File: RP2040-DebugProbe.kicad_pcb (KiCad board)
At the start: 2 copper layers, 60 parts, among them J1 CONN_MCU_JTAG, J10 CONN_USB, J2 CONN_MCU_UART, J3 CONN_DBG_COMB, J4 CONN_3V3_JUMPER, J7 CONN_DBG_JTAG, SW1 BOOTSEL, U1 W25Q128JVS, U2 RP2040, U3 74AUP1T17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

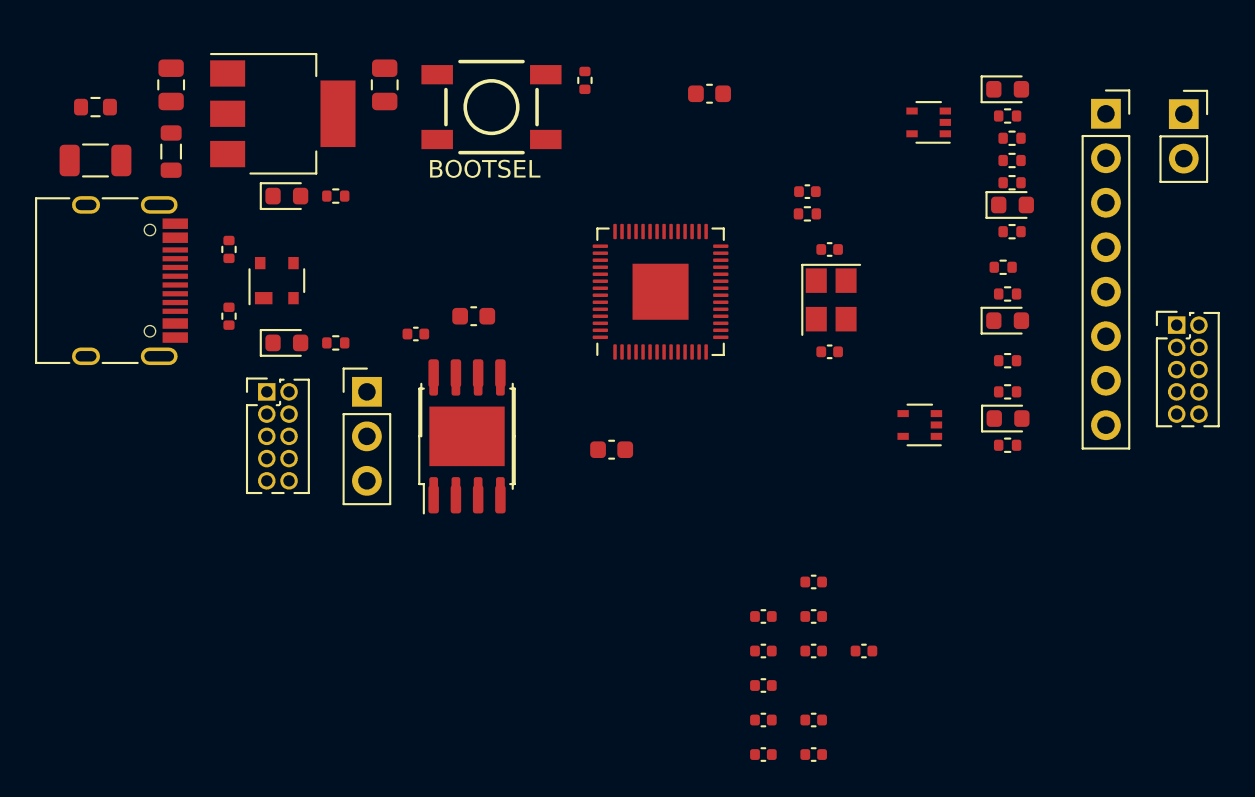
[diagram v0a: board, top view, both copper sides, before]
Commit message: Placed components on their approximate locations. Added board approximate outline.
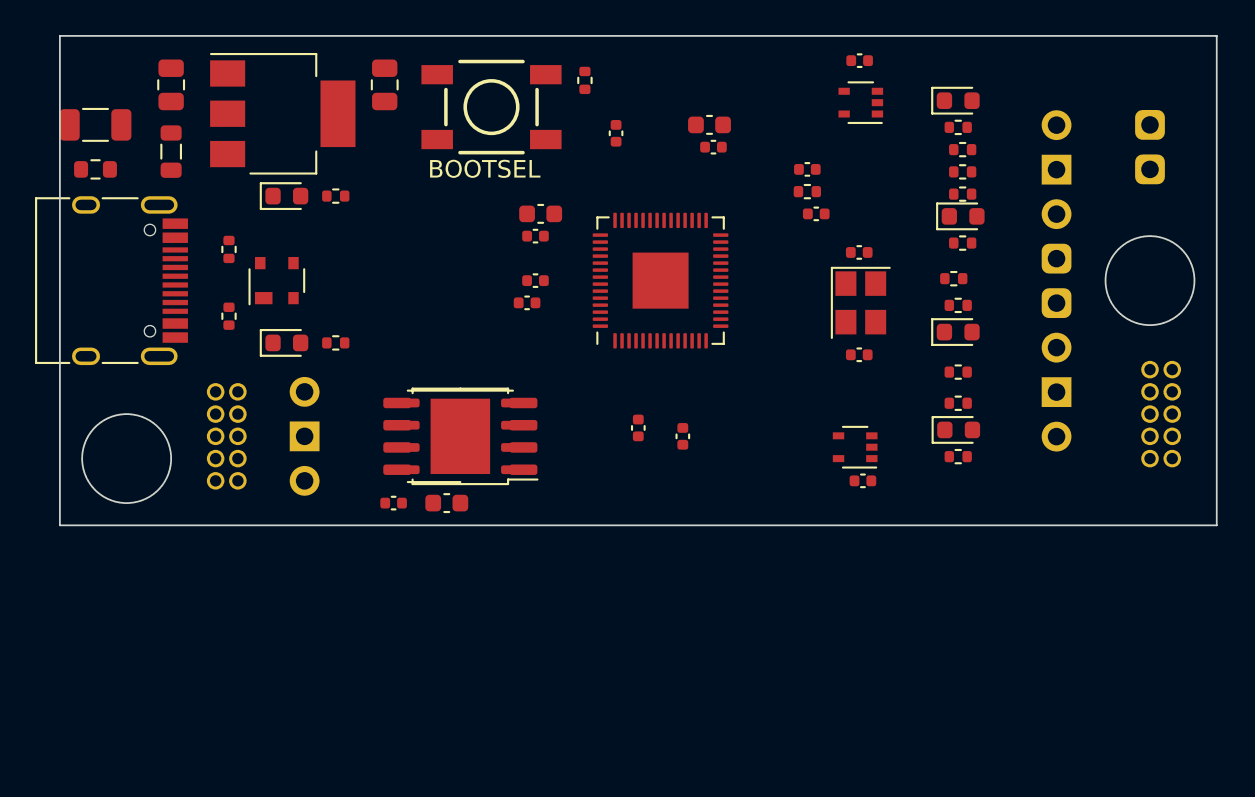
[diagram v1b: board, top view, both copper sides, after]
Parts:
- removed C22: 100nF, Capacitor_SMD:C_0402_1005Metric
- J3: footprint Connector_PinSocket_2.54mm:PinSocket_1x08_P2.54mm_Vertical -> Connector_PinHeader_2.54mm:PinHeader_1x08_P2.54mm_Vertical
- J4: footprint Connector_PinSocket_2.54mm:PinSocket_1x02_P2.54mm_Vertical -> Connector_PinHeader_2.54mm:PinHeader_1x02_P2.54mm_Vertical
- moved C17 39.7 mm to (170.1, 95.4)
- moved C6 32.6 mm to (156.2, 99.5), turned to 90 degrees
- moved C7 30.5 mm to (151.6, 105.4), turned to 180 degrees
- moved C8 30.0 mm to (151.6, 108.0), turned to 180 degrees
- moved C4 28.9 mm to (161.8, 100.3)
- moved C11 25.0 mm to (167.6, 104.1)
- moved C9 22.8 mm to (151.1, 109.2), turned to 180 degrees
- moved C5 14.1 mm to (151.9, 104.1), turned to 180 degrees
- moved C13 13.9 mm to (170.3, 119.4)
- moved C3 12.9 mm to (157.5, 116.4), turned to -90 degrees
- moved C10 12.7 mm to (160.0, 116.8), turned to -90 degrees
- moved C16 10.8 mm to (146.5, 120.7)
- moved C2 9.74 mm to (143.5, 120.7)
- moved J7 7.62 mm to (188.0, 118.1), turned to 180 degrees
- moved J1 5.34 mm to (134.6, 119.4), turned to 180 degrees
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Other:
- board outline added: 66 x 27.9 mm

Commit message: Moved stuff around
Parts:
- added C18: 100nF, Capacitor_SMD:C_0402_1005Metric, F.Cu at (164.5, 104.1)
- moved C1 17.5 mm to (158.1, 116.2), turned to -90 degrees
- moved R13 9.75 mm to (169.5, 115.6)
- moved C6 7.34 mm to (150.5, 104.1), turned to 180 degrees
- moved J7 6.99 mm to (181.0, 118.1)
- moved J3 6.73 mm to (174.6, 99.1)
- moved R15 6.60 mm to (169.5, 100.3)
- moved R9 6.55 mm to (169.5, 101.6)
- moved D1 6.48 mm to (169.5, 104.1)
- moved R1 6.46 mm to (169.5, 105.4), turned to 0 degrees
- moved R14 6.45 mm to (169.5, 102.9)
- moved R2 6.36 mm to (169.5, 97.8)
- moved J4 6.35 mm to (180.3, 99.1)
- moved D4 6.35 mm to (169.5, 99.1)
- moved R5 6.32 mm to (169.4, 118.1)
- moved R4 6.30 mm to (169.5, 110.5)
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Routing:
- net VUSB: track 0.00 -> 56.0 mm, vias 0 -> 1
- net +3V3: track 0.00 -> 48.5 mm, vias 0 -> 6
- net +1V1: track 0.00 -> 37.3 mm, vias 0 -> 3
- net QSPI_SS: track 0.00 -> 25.4 mm, vias 0 -> 2
- net USB_DP: track 0.00 -> 24.7 mm, vias 0 -> 2
- net USB_DN: track 0.00 -> 24.6 mm
- net VBUS: track 0.00 -> 20.6 mm, vias 0 -> 4
- net TARGET_3V3: track 0.00 -> 19.5 mm
- net QSPI_SD3: track 0.00 -> 16.6 mm
- net QSPI_SCLK: track 0.00 -> 14.5 mm
- net TARGET_CLK: track 0.00 -> 12.3 mm
- net SHIELD: track 0.00 -> 12.2 mm, vias 0 -> 1
- net TARGET_DIO: track 0.00 -> 12.0 mm
- net QSPI_SD0: track 0.00 -> 9.89 mm
- net XIN: track 0.00 -> 9.85 mm
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- added copper zone on B.Cu, net GND
- added copper zone on F.Cu, net GND
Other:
- board size 66 x 27.9 mm -> 59.7 x 25.4 mm

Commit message: Moved stuff around
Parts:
- moved C21 20.1 mm to (133.3, 117.5), turned to -90 degrees
- moved C1 14.6 mm to (157.5, 101.6), turned to 0 degrees
- moved R12 14.2 mm to (133.3, 114.3), turned to 0 degrees
- moved R3 11.4 mm to (130.2, 114.9)
- moved R6 11.4 mm to (130.2, 101.0)
- moved D2 9.16 mm to (130.2, 99.7), turned to 180 degrees
- moved D5 9.16 mm to (130.2, 116.2), turned to 180 degrees
- moved C16 9.05 mm to (155.6, 118.7), turned to 90 degrees
- moved C4 2.69 mm to (157.5, 102.9), turned to 0 degrees
- moved U1 2.69 mm to (149.2, 117.5)
- moved U4 2.69 mm to (149.2, 117.5)
- moved C10 1.91 mm to (158.8, 116.2)
- moved C14 1.91 mm to (145.4, 97.8)
- moved C15 1.91 mm to (133.3, 97.8)
- moved C3 1.91 mm to (155.6, 116.2)
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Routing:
- net +1V1: track 37.3 -> 10.3 mm
- net XIN: track 9.85 -> 0.00 mm
- net XOUT: track 7.01 -> 0.00 mm
- net SHIELD: track 12.2 -> 7.66 mm
- net +3V3: track 48.5 -> 44.1 mm, vias 6 -> 4
- net QSPI_SD2: track 7.23 -> 11.5 mm
- net QSPI_SD1: track 8.22 -> 12.3 mm
- net USB_DP: track 24.7 -> 21.6 mm
- net USB_DN: track 24.6 -> 21.5 mm
- net VUSB: track 56.0 -> 52.8 mm
- net Net-(R7-Pad1): track 9.05 -> 6.20 mm
- net Net-(D5-A): track 1.88 -> 0.00 mm
- net Net-(D2-A): track 1.88 -> 0.00 mm
- net QSPI_SD3: track 16.6 -> 15.1 mm
- net QSPI_SCLK: track 14.5 -> 12.9 mm
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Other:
- board size 59.7 x 25.4 mm -> 55.9 x 25.4 mm
- board text added: "3V3"
- board text added: "3V3 ON"
- board text added: "5V"
- board text added: "CLK"
- board text added: "CON"
- board text added: "DIO"
- board text added: "GND"
- board text added: "JTAG"
- board text added: "PWR"
- board text added: "RX"
- board text added: "SWD"
- board text added: "TX"
- board text added: "UART"
